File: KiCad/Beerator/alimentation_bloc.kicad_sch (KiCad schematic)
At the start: 9 parts

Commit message: feat(Kicad): Schemas V1
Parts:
- added SW?: SW_DPDT_x2, symbol Switch:SW_DPDT_x2
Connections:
- net 7.2: now also SW?.1 (A); no longer JBat1.2 (Pin_2)
- new net: JBat1.2 (Pin_2), SW?.2 (B)
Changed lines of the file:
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@@
+    (stroke (width 0) (type default) (color 0 0 0 0))
+  )
+  (wire (pts (xy 53.34 40.64) (xy 58.928 40.64))
     (stroke (width 0) (type default) (color 0 0 0 0))
   )
@@
     (stroke (width 0) (type default) (color 0 0 0 0))
   )
+  (wire (pts (xy 69.088 38.1) (xy 74.168 38.1))
+    (stroke (width 0) (type default) (color 0 0 0 0))
+  )
   (wire (pts (xy 161.29 92.71) (xy 161.29 100.33))
     (stroke (width 0) (type default) (color 0 0 0 0))
@@
   )
   (wire (pts (xy 149.86 96.52) (xy 149.86 92.71))
-    (stroke (width 0) (type default) (color 0 0 0 0))
-  )
-  (wire (pts (xy 53.34 40.64) (xy 62.23 40.64))
     (stroke (width 0) (type default) (color 0 0 0 0))
   )
@@
     )
   )
-  (global_label "7.2" (shape input) (at 62.23 40.64 0) (fields_autoplaced)
+  (global_label "7.2" (shape input) (at 74.168 38.1 0) (fields_autoplaced)
     (effects (font (size 1.27 1.27)) (justify left))
-    (property "Intersheet References" "${INTERSHEET_REFS}" (id 0) (at 67.6669 40.5606 0)
+    (property "Intersheet References" "${INTERSHEET_REFS}" (id 0) (at 79.6049 38.0206 0)
       (effects (font (size 1.27 1.27)) (justify left) hide)
     )
@@
   (symbol (lib_id "Connector:Conn_01x02_Female") (at 48.26 43.18 180) (unit 1)
     (in_bom yes) (on_board yes)
-    (property "Reference" "JBat1" (id 0) (at 49.53 33.02 0))
-    (property "Value" "Conn_01x02_Female" (id 1) (at 57.15 35.56 0))
+    (property "Reference" "JBat1" (id 0) (at 40.64 34.036 0))
+    (property "Value" "Conn_01x02_Female" (id 1) (at 48.26 36.576 0))
     (property "Footprint" "Connector_JST:JST_XH_B2B-XH-AM_1x02_P2.50mm_Vertical" (id 2) (at 48.26 43.18 0)
       (effects (font (size 1.27 1.27)) hide)
@@
     (pin "2")
   )
+  (symbol (lib_id "Switch:SW_DPDT_x2") (at 64.008 40.64 0) (unit 1)
+    (in_bom yes) (on_board yes) (fields_autoplaced)
+    (property "Reference" "SW?" (id 0) (at 64.008 32.512 0))
+    (property "Value" "SW_DPDT_x2" (id 1) (at 64.008 35.052 0))
+    (property "Footprint" "" (id 2) (at 64.008 40.64 0)
+      (effects (font (size 1.27 1.27)) hide)
+    )
+    (property "Datasheet" "~" (id 3) (at 64.008 40.64 0)
+      (effects (font (size 1.27 1.27)) hide)
+    )
+    (pin "1")
+    (pin "2")
+    (pin "3")
+    (pin "4")
+    (pin "5")
+    (pin "6")
+  )
   (symbol (lib_id "power:GND") (at 46.99 107.95 0) (unit 1)

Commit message: feat(KiCad): Version 2
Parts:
- added D101: LED_Small, symbol Device:LED_Small
- added R103: 215, symbol Device:R_Small
- gave numbers to parts that had none: 1
- renumbered C1 to C101, C2 to C102, R1 to R101, R2 to R102
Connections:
- net 7.2: now also R103.1
- net GND: now also D101.1 (K)
- new net: D101.2 (A), R103.2
- no-connect marks 0 -> 1
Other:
- note added: "3V 20mA"
- note added: "LED ALIMENTATION"
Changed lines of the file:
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@@
   (junction (at 149.86 102.87) (diameter 0) (color 0 0 0 0)
   )
+  (junction (at 71.374 38.1) (diameter 0) (color 0 0 0 0)
+  )
+  (no_connect (at 69.088 43.18))
   (wire (pts (xy 71.12 104.14) (xy 71.12 107.95))
     (stroke (width 0) (type default) (color 0 0 0 0))
@@
     (stroke (width 0) (type default) (color 0 0 0 0))
   )
+  (wire (pts (xy 170.942 31.115) (xy 169.291 31.115))
+    (stroke (width 0) (type default) (color 0 0 0 0))
+  )
   (wire (pts (xy 149.86 101.6) (xy 149.86 102.87))
     (stroke (width 0) (type default) (color 0 0 0 0))
   )
+  (wire (pts (xy 170.942 38.608) (xy 170.942 31.115))
+    (stroke (width 0) (type default) (color 0 0 0 0))
+  )
   (wire (pts (xy 179.07 110.49) (xy 179.07 115.57))
     (stroke (width 0) (type default) (color 0 0 0 0))
@@
     (stroke (width 0) (type default) (color 0 0 0 0))
   )
+  (polyline (pts (xy 197.993 71.12) (xy 197.993 11.938))
+    (stroke (width 0) (type default) (color 0 0 0 0))
+  )
   (wire (pts (xy 60.96 43.18) (xy 60.96 46.99))
     (stroke (width 0) (type default) (color 0 0 0 0))
   )
+  (wire (pts (xy 150.495 31.115) (xy 150.495 38.608))
+    (stroke (width 0) (type default) (color 0 0 0 0))
+  )
   (wire (pts (xy 149.86 92.71) (xy 161.29 92.71))
     (stroke (width 0) (type default) (color 0 0 0 0))
   )
+  (wire (pts (xy 71.374 32.639) (xy 71.374 38.1))
+    (stroke (width 0) (type default) (color 0 0 0 0))
+  )
   (polyline (pts (xy 234.95 71.12) (xy 234.95 129.54))
     (stroke (width 0) (type default) (color 0 0 0 0))
@@
     (stroke (width 0) (type default) (color 0 0 0 0))
   )
-  (wire (pts (xy 69.088 38.1) (xy 74.168 38.1))
+  (wire (pts (xy 69.088 38.1) (xy 71.374 38.1))
+    (stroke (width 0) (type default) (color 0 0 0 0))
+  )
+  (wire (pts (xy 155.575 31.115) (xy 164.211 31.115))
     (stroke (width 0) (type default) (color 0 0 0 0))
   )
@@
     (stroke (width 0) (type default) (color 0 0 0 0))
   )
+  (wire (pts (xy 71.374 38.1) (xy 74.168 38.1))
+    (stroke (width 0) (type default) (color 0 0 0 0))
+  )
   (polyline (pts (xy 118.11 129.54) (xy 120.65 129.54))
     (stroke (width 0) (type default) (color 0 0 0 0))
@@
   )
   (polyline (pts (xy 120.65 71.12) (xy 120.65 129.54))
+    (stroke (width 0) (type default) (color 0 0 0 0))
+  )
+  (polyline (pts (xy 197.866 11.938) (xy 197.993 11.938))
     (stroke (width 0) (type default) (color 0 0 0 0))
   )
@@
     (effects (font (size 1.27 1.27)) (justify left bottom))
   )
+  (text "3V\n20mA" (at 153.67 36.83 0)
+    (effects (font (size 1.27 1.27)) (justify left bottom))
+  )
+  (text "LED ALIMENTATION\n" (at 123.571 17.272 0)
+    (effects (font (size 1.27 1.27)) (justify left bottom))
+  )
   (text "Batterie Connector" (at 19.05 19.05 0)
     (effects (font (size 1.27 1.27)) (justify left bottom))
+  )
+  (global_label "ALIM_LED" (shape input) (at 71.374 32.639 90) (fields_autoplaced)
+    (effects (font (size 1.27 1.27)) (justify left))
+    (property "Intersheet References" "${INTERSHEET_REFS}" (id 0) (at 71.2946 21.6383 90)
+      (effects (font (size 1.27 1.27)) (justify left) hide)
+    )
   )
   (global_label "7.2" (shape input) (at 39.37 93.98 180) (fields_autoplaced)
@@
     )
   )
+  (global_label "ALIM_LED" (shape input) (at 170.942 38.608 270) (fields_autoplaced)
+    (effects (font (size 1.27 1.27)) (justify right))
+    (property "Intersheet References" "${INTERSHEET_REFS}" (id 0) (at 170.8626 49.6087 90)
+      (effects (font (size 1.27 1.27)) (justify right) hide)
+    )
+  )
   (global_label "5" (shape input) (at 78.74 93.98 0) (fields_autoplaced)
     (effects (font (size 1.27 1.27)) (justify left))
@@
     (pin "2")
   )
+  (symbol (lib_id "Device:LED_Small") (at 153.035 31.115 0) (unit 1)
+    (in_bom yes) (on_board yes) (fields_autoplaced)
+    (property "Reference" "D101" (id 0) (at 153.0985 24.13 0))
+    (property "Value" "LED_Small" (id 1) (at 153.0985 26.67 0))
+    (property "Footprint" "" (id 2) (at 153.035 31.115 90)
+      (effects (font (size 1.27 1.27)) hide)
+    )
+    (property "Datasheet" "~" (id 3) (at 153.035 31.115 90)
+      (effects (font (size 1.27 1.27)) hide)
+    )
+    (pin "1")
+    (pin "2")
+  )
   (symbol (lib_id "power:GND") (at 60.96 46.99 0) (unit 1)
     (in_bom yes) (on_board yes) (fields_autoplaced)
@@
   (symbol (lib_id "Device:C_Small") (at 71.12 101.6 0) (unit 1)
     (in_bom yes) (on_board yes) (fields_autoplaced)
-    (property "Reference" "C2" (id 0) (at 73.66 100.3362 0)
+    (property "Reference" "C102" (id 0) (at 73.66 100.3362 0)
       (effects (font (size 1.27 1.27)) (justify left))
     )
@@
   (symbol (lib_id "Device:C_Small") (at 46.99 101.6 0) (unit 1)
     (in_bom yes) (on_board yes) (fields_autoplaced)
-    (property "Reference" "C1" (id 0) (at 49.53 100.3362 0)
+    (property "Reference" "C101" (id 0) (at 49.53 100.3362 0)
       (effects (font (size 1.27 1.27)) (justify left))
     )
@@
     )
     (property "Datasheet" "" (id 3) (at 189.23 115.57 0)
+      (effects (font (size 1.27 1.27)) hide)
+    )
+    (pin "1")
+  )
+  (symbol (lib_id "power:GND") (at 150.495 38.608 0) (unit 1)
+    (in_bom yes) (on_board yes) (fields_autoplaced)
+    (property "Reference" "#PWR0123" (id 0) (at 150.495 44.958 0)
+      (effects (font (size 1.27 1.27)) hide)
+    )
+    (property "Value" "GND" (id 1) (at 150.495 43.18 0))
+    (property "Footprint" "" (id 2) (at 150.495 38.608 0)
+      (effects (font (size 1.27 1.27)) hide)
+    )
+    (property "Datasheet" "" (id 3) (at 150.495 38.608 0)
       (effects (font (size 1.27 1.27)) hide)
     )
@@
   (symbol (lib_id "Device:R_Small") (at 149.86 110.49 0) (unit 1)
     (in_bom yes) (on_board yes) (fields_autoplaced)
-    (property "Reference" "R2" (id 0) (at 152.4 109.2199 0)
+    (property "Reference" "R102" (id 0) (at 152.4 109.2199 0)
       (effects (font (size 1.27 1.27)) (justify left))
     )
@@
   (symbol (lib_id "Switch:SW_DPDT_x2") (at 64.008 40.64 0) (unit 1)
     (in_bom yes) (on_board yes) (fields_autoplaced)
-    (property "Reference" "SW?" (id 0) (at 64.008 32.512 0))
+    (property "Reference" "SW1" (id 0) (at 64.008 32.512 0))
     (property "Value" "SW_DPDT_x2" (id 1) (at 64.008 35.052 0))
     (property "Footprint" "" (id 2) (at 64.008 40.64 0)
@@
   (symbol (lib_id "Device:R_Small") (at 149.86 99.06 0) (unit 1)
     (in_bom yes) (on_board yes) (fields_autoplaced)
-    (property "Reference" "R1" (id 0) (at 152.4 97.7899 0)
+    (property "Reference" "R101" (id 0) (at 152.4 97.7899 0)
       (effects (font (size 1.27 1.27)) (justify left))
     )
@@
     (pin "1")
   )
+  (symbol (lib_id "Device:R_Small") (at 166.751 31.115 270) (unit 1)
+    (in_bom yes) (on_board yes) (fields_autoplaced)
+    (property "Reference" "R103" (id 0) (at 166.751 25.4 90))
+    (property "Value" "215" (id 1) (at 166.751 27.94 90))
+    (property "Footprint" "" (id 2) (at 166.751 31.115 0)
+      (effects (font (size 1.27 1.27)) hide)
+    )
+    (property "Datasheet" "~" (id 3) (at 166.751 31.115 0)
+      (effects (font (size 1.27 1.27)) hide)
+    )
+    (pin "1")
+    (pin "2")
+  )
 )

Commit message: feat(last pcb version)
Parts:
- removed R101: 3meg, Resistor_SMD:R_0603_1608Metric_Pad0.98x0.95mm_HandSolder, symbol Device:R_Small
- removed R102: 1,5meg, Resistor_SMD:R_0603_1608Metric_Pad0.98x0.95mm_HandSolder, symbol Device:R_Small
- added D102: LED_Small, LED_SMD:LED_0603_1608Metric_Pad1.05x0.95mm_HandSolder, symbol Device:LED_Small
- added R105: 215, Resistor_SMD:R_0603_1608Metric_Pad0.98x0.95mm_HandSolder, symbol Device:R_Small
- C103: renamed from C3; value 10u -> 1uF
- C104: renamed from C4; value 10u -> 1uF
- D101: footprint (none) -> LED_SMD:LED_0603_1608Metric_Pad1.05x0.95mm_HandSolder
- R103: footprint (none) -> Resistor_SMD:R_0603_1608Metric_Pad0.98x0.95mm_HandSolder
- SW1: footprint (none) -> SamacSys_Parts:NE555DR
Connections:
- net 3.3: now also R105.1
- net 5: now also C104.2, REG3-3.3 (~{SHDN}); no longer C104.1
- net GND: now also C104.1, D102.1 (K); no longer C104.2
- new net: D102.2 (A), R105.2
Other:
- note added: "C103,C104 -> Ceramic"
- moved on the sheet: C104

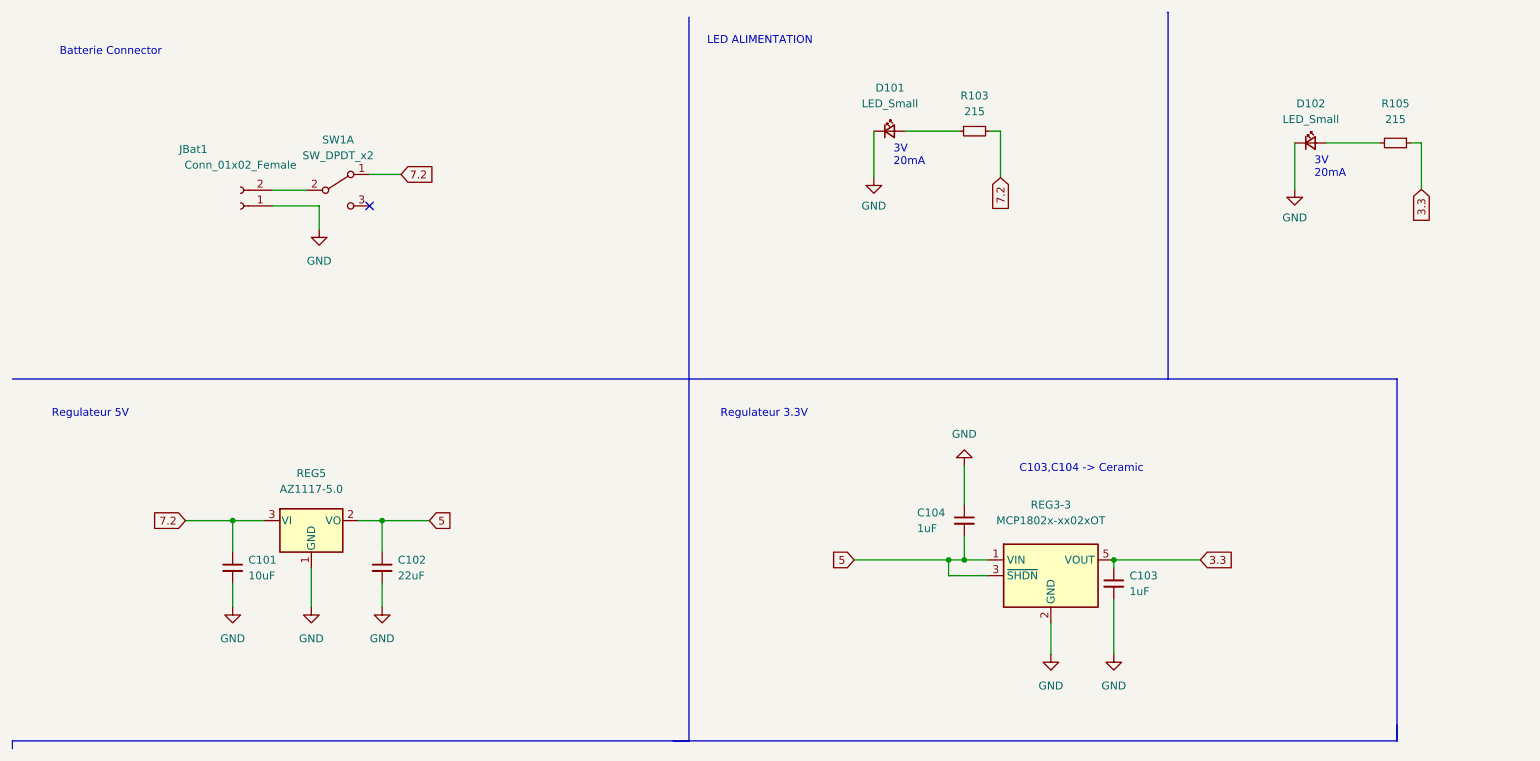
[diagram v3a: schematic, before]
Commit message: Dimensionement Led
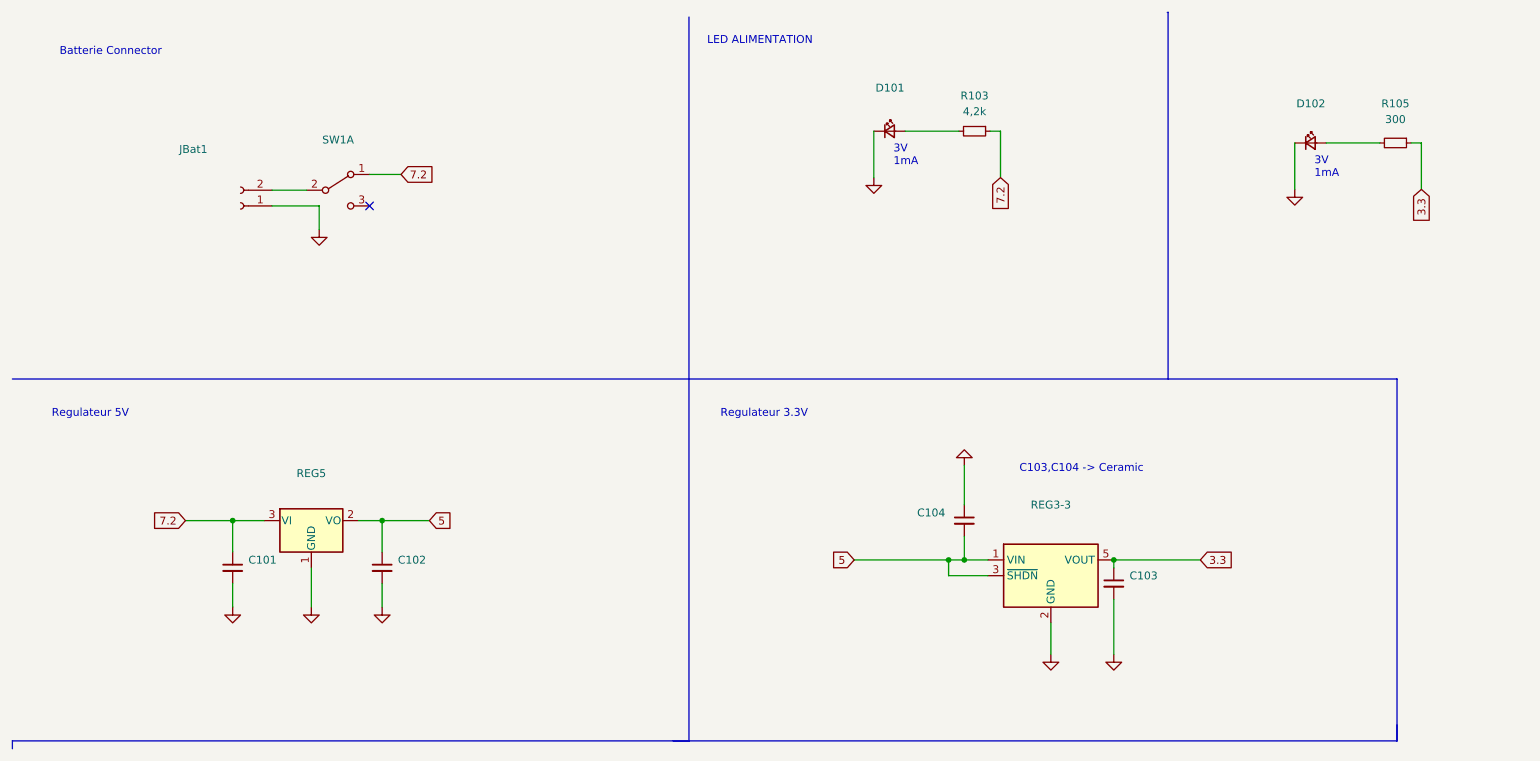
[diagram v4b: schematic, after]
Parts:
- C101: value 10uF -> (none); footprint Capacitor_SMD:C_0603_1608Metric_Pad1.08x0.95mm_HandSolder -> (none)
- C102: value 22uF -> (none); footprint Capacitor_SMD:C_0603_1608Metric_Pad1.08x0.95mm_HandSolder -> (none)
- C103, C104: value 1uF -> (none); footprint Capacitor_SMD:C_0603_1608Metric_Pad1.08x0.95mm_HandSolder -> (none)
- D101, D102: value LED_Small -> (none); footprint LED_SMD:LED_0603_1608Metric_Pad1.05x0.95mm_HandSolder -> (none)
- JBat1: value Conn_01x02_Female -> (none); footprint Connector_JST:JST_XH_B2B-XH-AM_1x02_P2.50mm_Vertical -> (none)
- R103: value 215 -> 4,2k; footprint Resistor_SMD:R_0603_1608Metric_Pad0.98x0.95mm_HandSolder -> (none)
- R105: value 215 -> 300; footprint Resistor_SMD:R_0603_1608Metric_Pad0.98x0.95mm_HandSolder -> (none)
- REG3-3: value MCP1802x-xx02xOT -> (none); footprint Package_TO_SOT_SMD:SOT-23-5 -> (none)
- REG5: value AZ1117-5.0 -> (none); footprint Package_TO_SOT_SMD:SOT-223 -> (none)
- SW1: value SW_DPDT_x2 -> (none); footprint SamacSys_Parts:NE555DR -> (none)
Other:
- note added: "3V 1mA"
- note removed: "3V 20mA"

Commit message: Update_Schemas
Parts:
- removed C103: (no value), symbol Device:C_Small
- added C204: 1uF, Capacitor_SMD:C_0603_1608Metric_Pad1.08x0.95mm_HandSolder, symbol Device:C_Small
- C201: renamed from C101; value (none) -> 10uF; footprint (none) -> Capacitor_SMD:C_0603_1608Metric_Pad1.08x0.95mm_HandSolder
- C202: renamed from C102; value (none) -> 22uF; footprint (none) -> Capacitor_SMD:C_0603_1608Metric_Pad1.08x0.95mm_HandSolder
- C203: renamed from C104; value (none) -> 1uF; footprint (none) -> Capacitor_SMD:C_0603_1608Metric_Pad1.08x0.95mm_HandSolder
- D201: renamed from D101; value (none) -> LED_Small; footprint (none) -> LED_SMD:LED_0603_1608Metric_Pad1.05x0.95mm_HandSolder
- D202: renamed from D102; value (none) -> LED_Small; footprint (none) -> LED_SMD:LED_0603_1608Metric_Pad1.05x0.95mm_HandSolder
- JBat201: renamed from JBat1; value (none) -> Conn_01x02_Female; footprint (none) -> Connector_JST:JST_XH_B2B-XH-AM_1x02_P2.50mm_Vertical
- R201: renamed from R103; footprint (none) -> Resistor_SMD:R_0603_1608Metric_Pad0.98x0.95mm_HandSolder
- R202: renamed from R105; footprint (none) -> Resistor_SMD:R_0603_1608Metric_Pad0.98x0.95mm_HandSolder
- REG201: renamed from REG5; value (none) -> AZ1117-5.0; footprint (none) -> Package_TO_SOT_SMD:SOT-223
- REG3-201: renamed from REG3-3; value (none) -> MCP1802x-xx02xOT; footprint (none) -> Package_TO_SOT_SMD:SOT-23-5
- SW201: renamed from SW1; value (none) -> SW_DPDT_x2; footprint (none) -> SamacSys_Parts:NE555DR
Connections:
- net GND: now also C203.2, C204.2; no longer C203.1
- net 3.3 renamed +3.3V
- net +3.3V: now also C204.1
- net 5 renamed +5V
- net +5V: now also C203.1; no longer C203.2
- net 7.2 renamed +BATT
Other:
- note added: "LED ALIMENTATION 3V"
- note added: "LED ALIMENTATION BATT"
- note removed: "LED ALIMENTATION"
- moved on the sheet: C203, D201, R201, R202

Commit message: version_finale_pcb
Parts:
- removed REG201: AZ1117-5.0, Package_TO_SOT_SMD:SOT-223, symbol Regulator_Linear:AZ1117-5.0
- added U201: REG-5, Package_TO_SOT_SMD:SOT-223, symbol Sensors_Beerator:REG-5
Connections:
- net +5V: now also U201.3 (OUT)
- net +BATT: now also U201.1 (Vin)
- net GND: now also U201.2 (GND), U201.4 (GND)
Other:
- moved on the sheet: C201, C202
